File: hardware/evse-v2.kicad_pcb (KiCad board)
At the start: 4 copper layers, 74 x 114 mm, 145 parts, among them J101 Boot, P101 CON-SENSOR2, P102 Relay, P103 L'+PE, P104 L'+PE, P105 CP/PP/PE, P106 Power, P107 Motor, P108 Switch_LED, P109 Enable, P110 MODBUS, P111 Debug, P112 DC-Protect, P113 GP, Q101 2N7002P, Q102 SI2305CDS-T1-GE3, Q103 2N7002P, Q104 2N7002P, Q105 SSM3J355R,LF, SW101 OS103011MS8QP1, SW102 OS103011MS8QP1, U101 XMC1404, U102 PEM1-S12-D12-S, U103 DMMT5401, U105 OPA171AIDBV, U106 A5950GLP, U108 AQH3213AX, U109 HCPL2731, U110 TPS70933DBVR, U111 IRM02-12, U112 WPMDL110, U113 SP3491, X101 16MHz

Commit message: change rs485 bias resistor values
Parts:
- R134, R136: value 2.7k -> 750
- R135: value 2.2k -> DNP

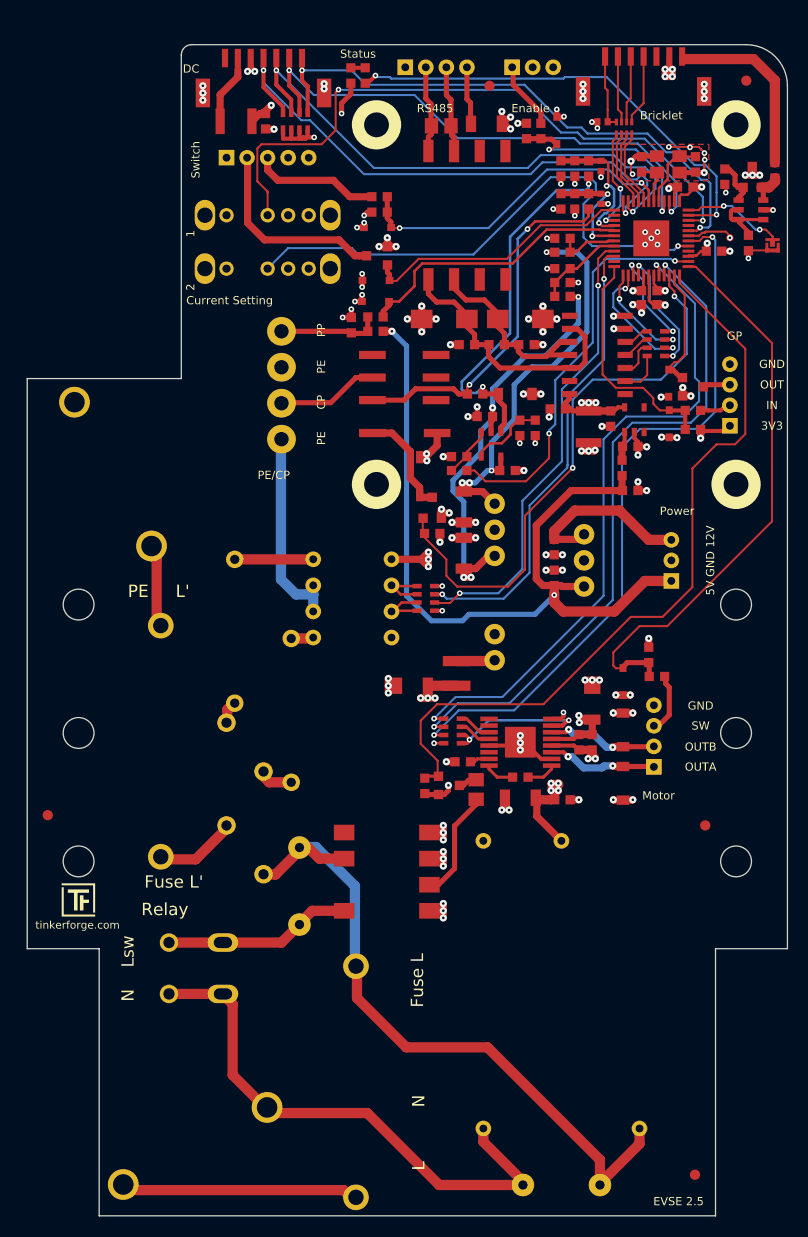
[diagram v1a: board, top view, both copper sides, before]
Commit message: change drill diameters
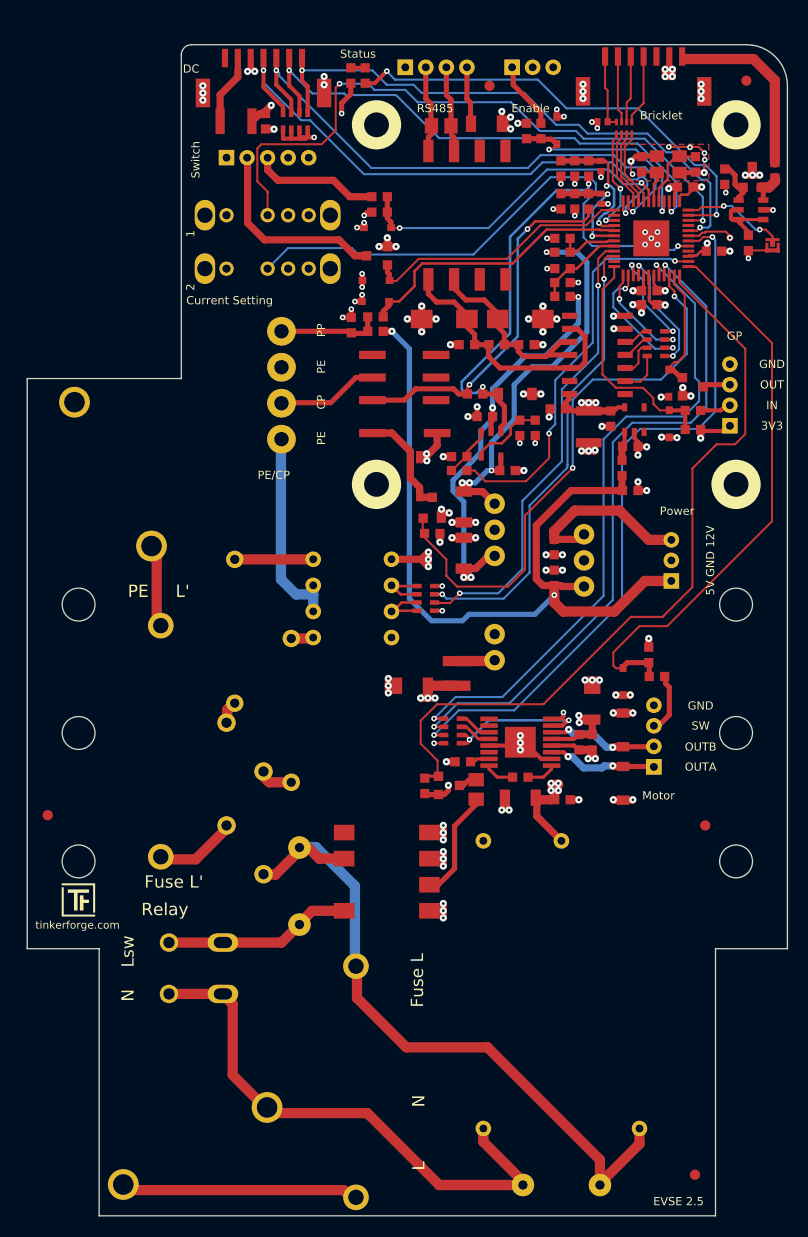
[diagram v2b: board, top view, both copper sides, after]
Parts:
- A101, A102, A103, A104: footprint kicad-libraries:DRILL_NP -> kicad-libraries:DRILL_NP_35
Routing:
- net GND: track 172.6 -> 173.7 mm
- net P0_5: track 62.8 -> 63.6 mm

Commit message: evse with testpoints
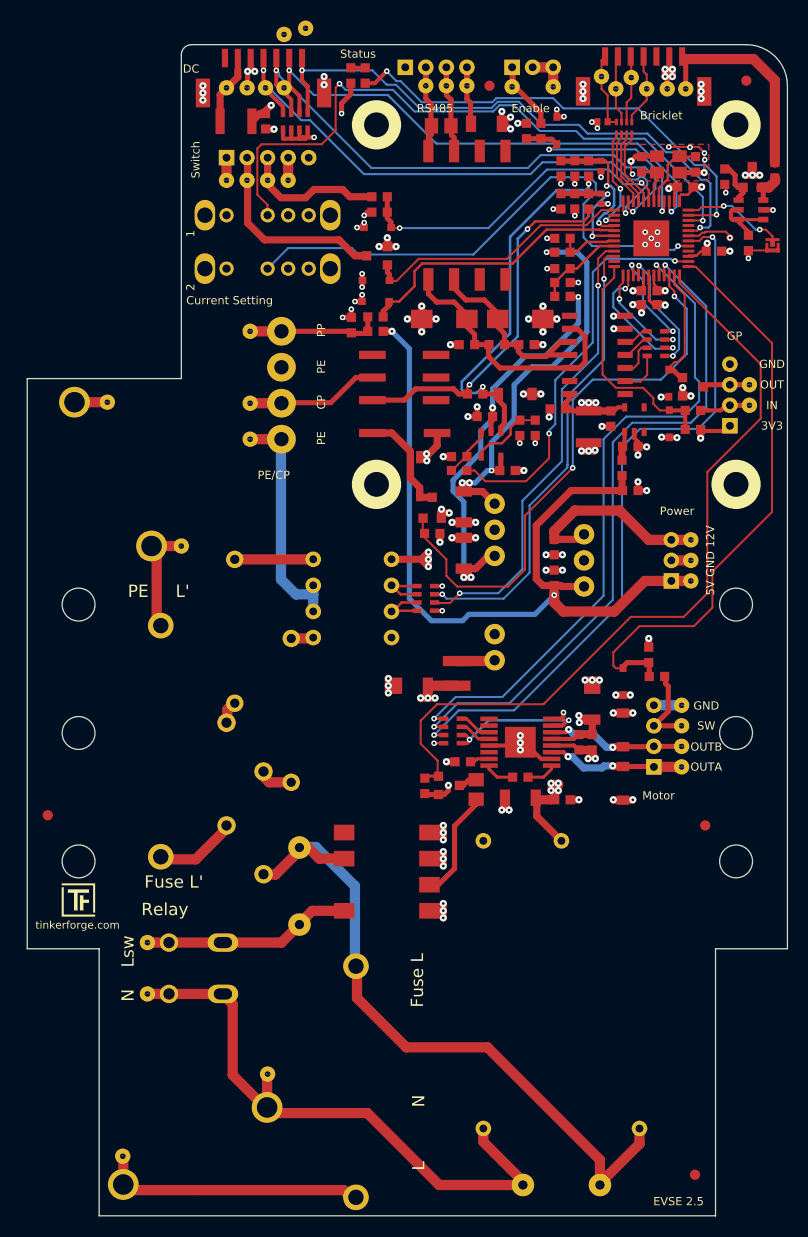
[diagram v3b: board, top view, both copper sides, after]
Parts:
- added P1: TP VCCPWR, kicad-libraries:TSTPT, F.Cu at (141.9, 99.8)
- added P10: TP DC-X6, kicad-libraries:TSTPT, F.Cu at (102.3, 55.8)
- added P11: TP DC-X30, kicad-libraries:TSTPT, F.Cu at (100.5, 55.8)
- added P12: TP PE, kicad-libraries:TSTPT, F.Cu at (85.2, 86.3)
- added P13: TP L', kicad-libraries:TSTPT, F.Cu at (92.3, 100.3)
- added P14: TP A, kicad-libraries:TSTPT, F.Cu at (116.2, 55.5)
- added P15: TP B, kicad-libraries:TSTPT, F.Cu at (118.2, 55.5)
- added P16: TP 5V, kicad-libraries:TSTPT, F.Cu at (141.4, 55.9)
- added P17: TP GND, kicad-libraries:TSTPT, F.Cu at (139.7, 55.9)
- added P18: TP CS, kicad-libraries:TSTPT, F.Cu at (137.7, 55.9)
- added P19: TP CLK, kicad-libraries:TSTPT, F.Cu at (136.2, 54.8)
- added P2: TP 5V, kicad-libraries:TSTPT, F.Cu at (141.9, 103.8)
- added P20: TP MOSI, kicad-libraries:TSTPT, F.Cu at (134.7, 55.9)
- added P21: TP MISO, kicad-libraries:TSTPT, F.Cu at (133.2, 54.6)
- added P22: TP GND, kicad-libraries:TSTPT, F.Cu at (120.2, 55.5)
- added P23: TP N, kicad-libraries:TSTPT, F.Cu at (89.0, 143.9)
- added P24: TP REL, kicad-libraries:TSTPT, F.Cu at (89.0, 138.9)
- added P25: TP OUTA, kicad-libraries:TSTPT, F.Cu at (141.1, 121.8)
- added P26: TP OUTB, kicad-libraries:TSTPT, F.Cu at (141.1, 119.8)
- added P27: TP M SW, kicad-libraries:TSTPT, F.Cu at (141.1, 117.8)
- added P28: TP GND, kicad-libraries:TSTPT, F.Cu at (141.1, 115.8)
- added P29: TP EN, kicad-libraries:TSTPT, F.Cu at (124.5, 55.6)
- added P3: TP GND, kicad-libraries:TSTPT, F.Cu at (141.9, 101.8)
- added P30: TP GND, kicad-libraries:TSTPT, F.Cu at (128.6, 55.6)
- added P31: TP VCCPWR, kicad-libraries:TSTPT, F.Cu at (96.8, 64.8)
- added P32: TP GND, kicad-libraries:TSTPT, F.Cu at (102.8, 64.8)
- added P33: TP SW, kicad-libraries:TSTPT, F.Cu at (100.8, 64.8)
- added P34: TP SWLED, kicad-libraries:TSTPT, F.Cu at (98.8, 64.8)
- added P35: TP GPIO IN, kicad-libraries:TSTPT, F.Cu at (147.7, 86.7)
- added P36: TP GPIO OUT, kicad-libraries:TSTPT, F.Cu at (147.7, 84.7)
- added P37: TP CP, kicad-libraries:TSTPT, F.Cu at (99.0, 86.5)
- added P38: TP PE, kicad-libraries:TSTPT, F.Cu at (99.0, 90.0)
- added P39: TP PP, kicad-libraries:TSTPT, F.Cu at (99.0, 79.5)
- added P4: TP L, kicad-libraries:TSTPT, F.Cu at (86.7, 159.8)
- added P5: TP DC-5V, kicad-libraries:TSTPT, F.Cu at (96.8, 55.8)
- added P6: TP N, kicad-libraries:TSTPT, F.Cu at (100.8, 151.8)
- added P7: TP GND, kicad-libraries:TSTPT, F.Cu at (98.8, 55.8)
- added P8: TP DC-ERR, kicad-libraries:TSTPT, F.Cu at (104.5, 50.0)
- added P9: TP DC-TST, kicad-libraries:TSTPT, F.Cu at (102.3, 50.5)
- P103: value L'+PE -> N+L
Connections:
- net 485-~REB renamed 485-~{REB}
- net ~MOTOR_FAULT renamed ~{MOTOR_FAULT}
- L104 pad 3: Net-(L104-Pad3) -> unconnected-(L104-Pad3)
- L104 pad 4: Net-(L104-Pad4) -> unconnected-(L104-Pad4)
- L104 pad 5: Net-(L104-Pad5) -> unconnected-(L104-Pad5)
- L104 pad 6: Net-(L104-Pad6) -> unconnected-(L104-Pad6)
- P101 pad 3: Net-(P101-Pad3) -> unconnected-(P101-Pad3)
- P112 pad 7: Net-(P112-Pad7) -> unconnected-(P112-Pad7)
- REL101 pad 2: Net-(REL101-Pad2) -> unconnected-(REL101-Pad2)
- REL101 pad 3: Net-(REL101-Pad3) -> unconnected-(REL101-Pad3)
- REL101 pad 4: Net-(REL101-Pad4) -> unconnected-(REL101-Pad4)
- REL101 pad 5: Net-(REL101-Pad5) -> unconnected-(REL101-Pad5)
- SW101 pad 3: Net-(SW101-Pad3) -> unconnected-(SW101-Pad3)
- SW102 pad 3: Net-(SW102-Pad3) -> unconnected-(SW102-Pad3)
- U101 pad 11: Net-(U101-Pad11) -> unconnected-(U101-Pad11)
- U101 pad 2: Net-(U101-Pad2) -> unconnected-(U101-Pad2)
- U101 pad 28: Net-(U101-Pad28) -> unconnected-(U101-Pad28)
- U101 pad 33: Net-(U101-Pad33) -> unconnected-(U101-Pad33)
- U106 pad 10: Net-(U106-Pad10) -> unconnected-(U106-Pad10)
- U106 pad 14: Net-(U106-Pad14) -> unconnected-(U106-Pad14)
- U106 pad 9: Net-(U106-Pad9) -> unconnected-(U106-Pad9)
- U108 pad 5: Net-(U108-Pad5) -> unconnected-(U108-Pad5)
- U110 pad 3: Net-(U110-Pad3) -> unconnected-(U110-Pad3)
- U110 pad 4: Net-(U110-Pad4) -> unconnected-(U110-Pad4)
- U113 pad 1: Net-(U113-Pad1) -> unconnected-(U113-Pad1)
- U113 pad 13: Net-(U113-Pad13) -> unconnected-(U113-Pad13)
- U113 pad 8: Net-(U113-Pad8) -> unconnected-(U113-Pad8)
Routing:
- net GND: track 173.7 -> 193.6 mm
- net N: track 53.4 -> 58.8 mm
- net VCC: track 224.8 -> 229.9 mm
- net Net-(L103-Pad2): track 20.9 -> 24.2 mm
- net Net-(P105-Pad4): track 10.2 -> 13.2 mm
- net CPOUT2: track 9.86 -> 12.9 mm
- net Net-(F102-Pad1): track 7.66 -> 10.6 mm
- net Net-(F101-Pad1): track 23.1 -> 25.9 mm
- net Net-(D109-Pad1): track 10.8 -> 13.5 mm
- net Net-(D108-Pad1): track 10.7 -> 13.4 mm
- net Net-(P107-Pad3): track 5.87 -> 8.22 mm
- net Net-(P102-Pad1): track 18.7 -> 20.8 mm
- net 5V: track 265.1 -> 267.0 mm
- net Net-(P113-Pad2): track 3.06 -> 4.96 mm
- net Net-(P113-Pad3): track 2.72 -> 4.62 mm
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- added copper zone on In2.Cu, net 3V3
- added copper zone on In1.Cu, net GND
- removed copper zone on VCC.Cu, net 3V3
- removed copper zone on GND.Cu, net GND
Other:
- net class Default removed

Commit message: ready for review
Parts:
- moved P9 5.25 mm to (103.0, 55.8)
- moved P8 4.70 mm to (104.5, 54.6)
- moved P10 1.36 mm to (101.5, 54.6)
- moved P7 0.70 mm to (98.0, 55.8)
- moved P11 0.60 mm to (100.0, 55.8)
- moved P5 0.60 mm to (96.2, 55.8)
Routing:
- net 5V: track 267.0 -> 270.1 mm
- net DC-TST: track 52.1 -> 51.2 mm, vias 2 -> 1
- net DC-X6: track 53.8 -> 54.5 mm, vias 2 -> 1
- net DC-X30: track 55.0 -> 54.3 mm, vias 2 -> 1
- net DC-ERR: track 56.8 -> 56.6 mm, vias 2 -> 1

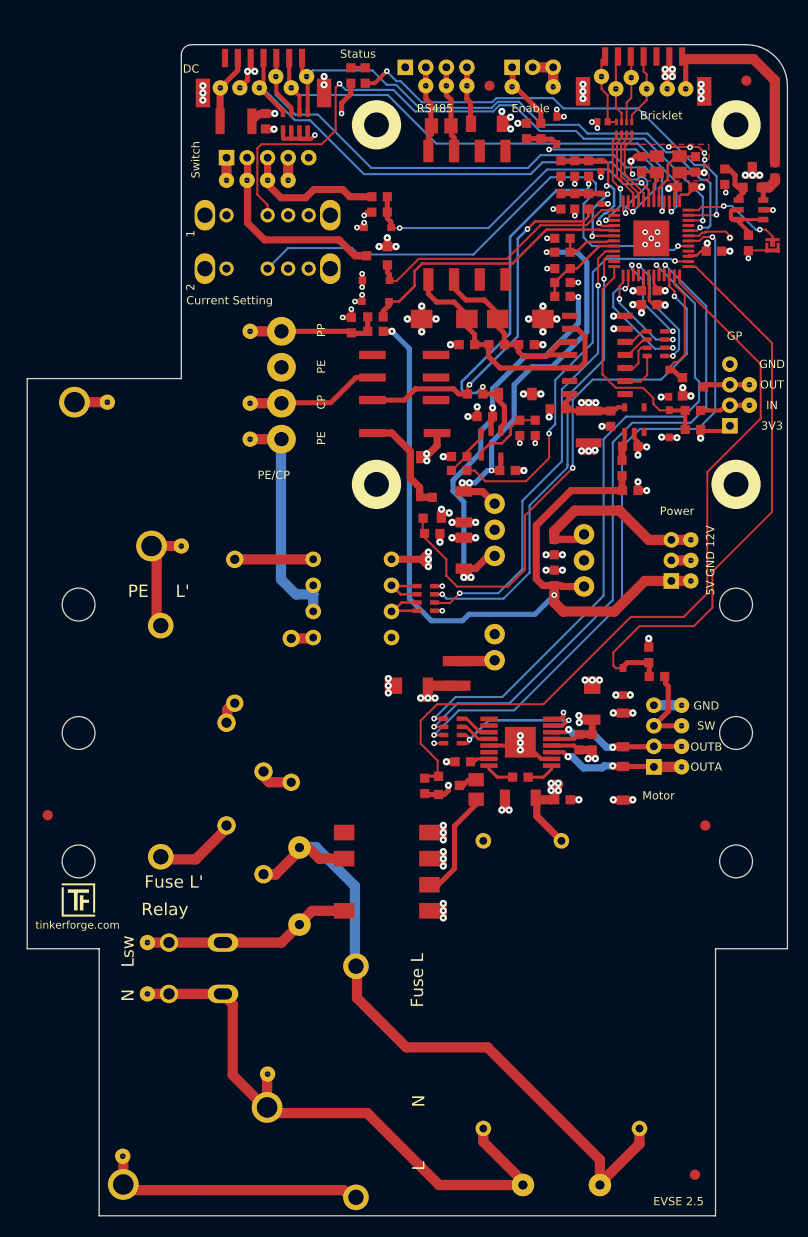
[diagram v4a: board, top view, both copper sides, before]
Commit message: Version 2.7: Changed L103 to 0 Ohm resistor.
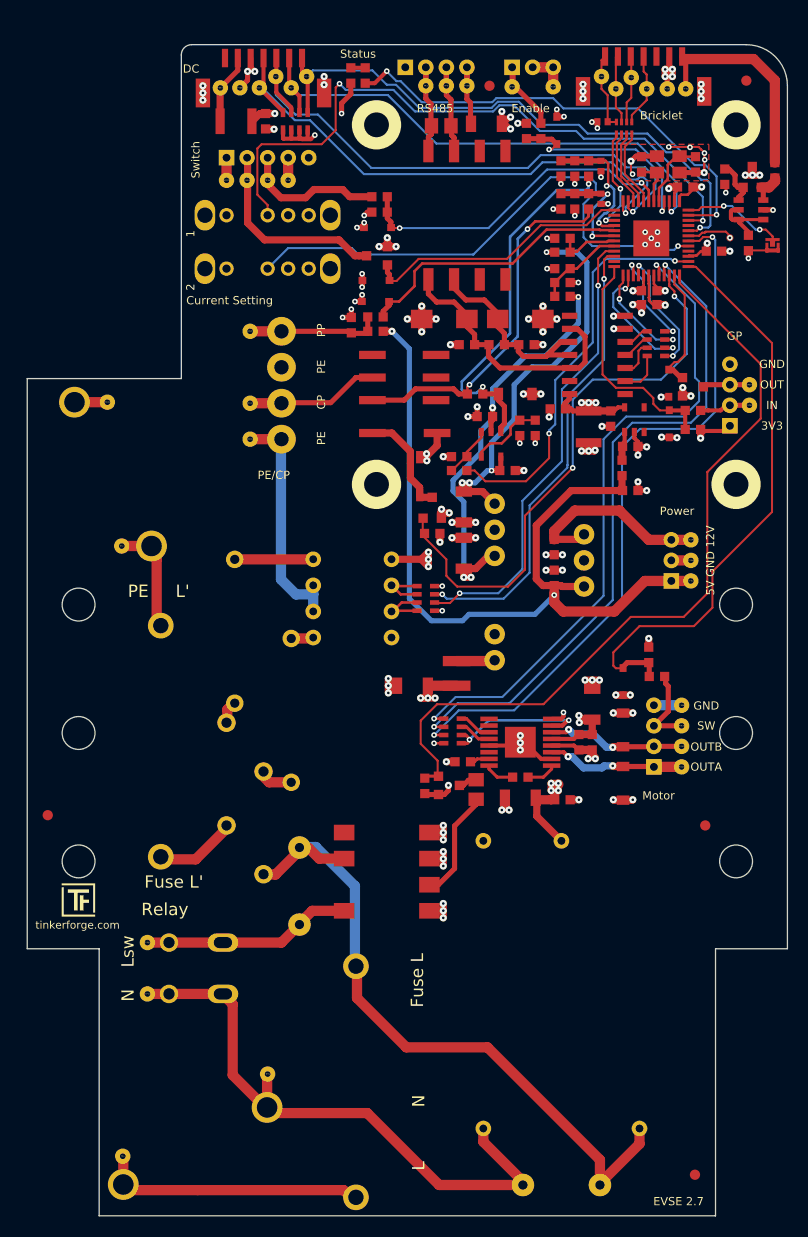
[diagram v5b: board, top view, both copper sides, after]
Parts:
- removed L105: 744032221, kicad-libraries:1210
- added R1: 0, kicad-libraries:R1210, F.Cu at (97.7, 59.0)
- moved P13 5.80 mm to (86.5, 100.3)
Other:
- board text added: "EVSE 2.7"
- board text removed: "EVSE 2.5"

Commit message: change varistor
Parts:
- R113, R128: value MOV-10D391KTR -> MOV-10D431K
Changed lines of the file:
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@@
       (effects (font (size 0.3 0.3) (thickness 0.075)))
     )
-    (fp_text value "MOV-10D391KTR" (at 0.05 0.2) (layer "F.Fab")
+    (fp_text value "MOV-10D431K" (at 0.05 0.2) (layer "F.Fab")
       (effects (font (size 0.3 0.3) (thickness 0.075)))
     )
@@
       (effects (font (size 0.3 0.3) (thickness 0.075)))
     )
-    (fp_text value "MOV-10D391KTR" (at 0.05 0.2 90) (layer "F.Fab")
+    (fp_text value "MOV-10D431K" (at 0.05 0.2 90) (layer "F.Fab")
       (effects (font (size 0.3 0.3) (thickness 0.075)))
     )
